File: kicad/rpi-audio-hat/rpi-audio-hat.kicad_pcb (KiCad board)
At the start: 2 copper layers, 65 x 57.6 mm, 14 parts, among them J1 Raspberry_Pi_2_3, J2 Conn_02x20_Counter_Clockwise, J4 Conn_Volume_Slider, J5 Screw_Terminal_01x02, J6 Screw_Terminal_01x02, J7 Screw_Terminal_01x02, SW1 SW_SPDT, U1 PCM5102_breakout, U2 PAM8302A_Adafruit_Board

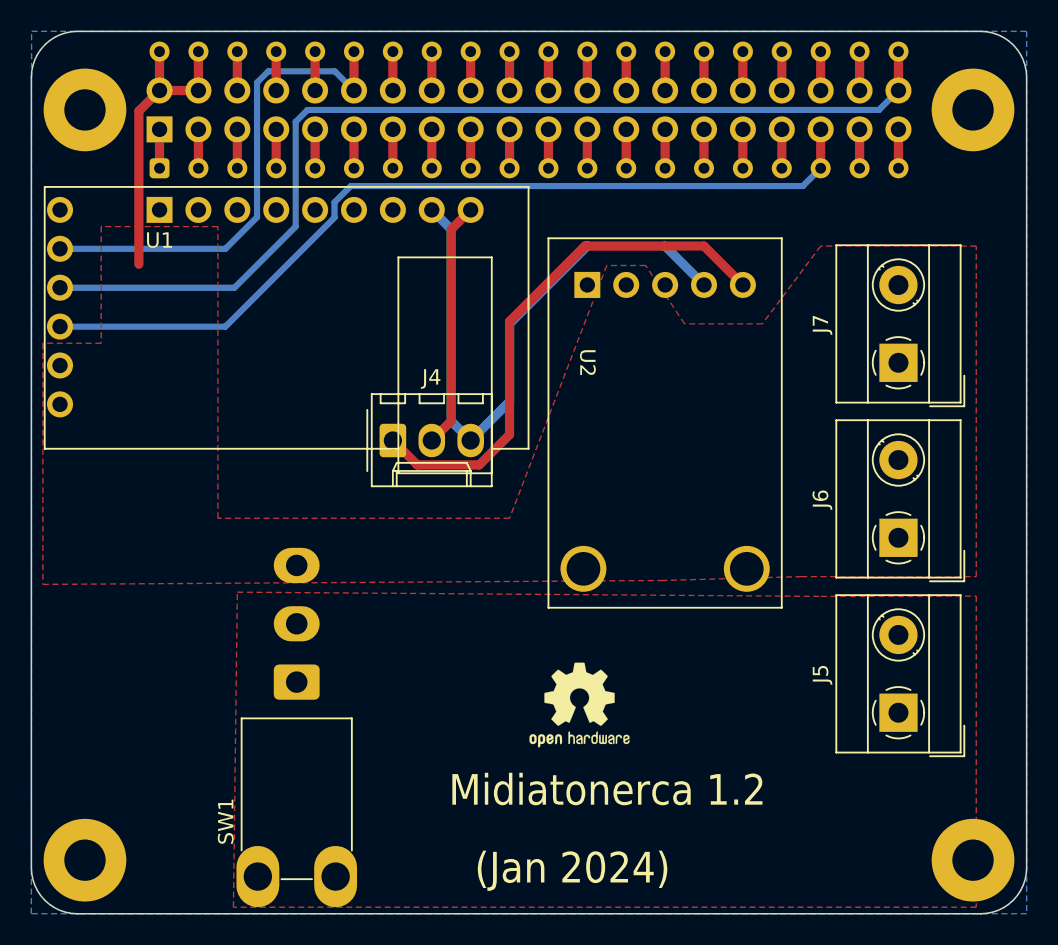
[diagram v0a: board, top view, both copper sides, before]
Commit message: Update PCB for RPi audio hat
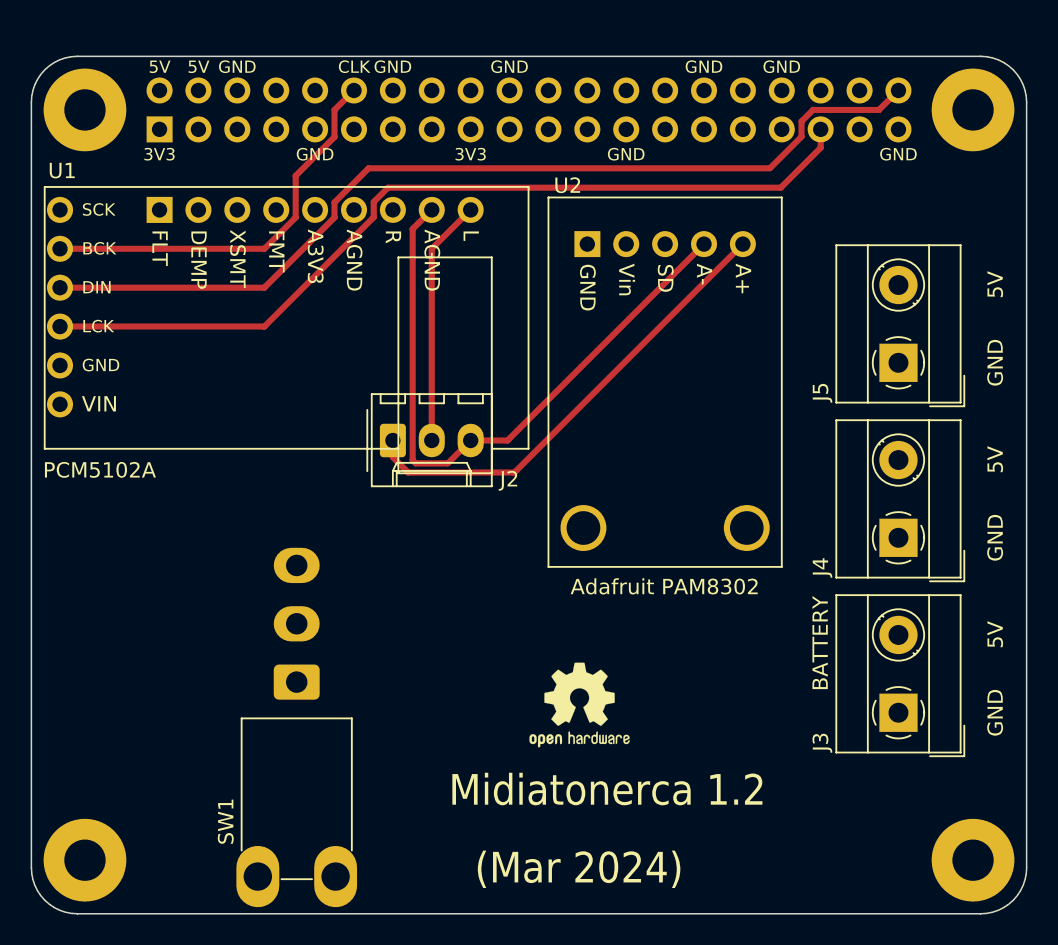
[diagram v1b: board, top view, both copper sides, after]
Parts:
- removed the J2 at (25.4, 27.9)
- U1: footprint Audio_Module:PCM5102_breakout -> MidiatonercaLibrary:PCM5102_breakout
- U2: footprint Audio_Module:PAM8302 -> MidiatonercaLibrary:PAM8302
- moved U2 2.67 mm to (53.3, 32.9)
- renumbered J4 to J2, J5 to J3, J6 to J4, J7 to J5
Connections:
- J1 pad 10: rpi10 -> unconnected-(J1-GPIO15/RXD-Pad10)
- J1 pad 11: rpi11 -> unconnected-(J1-GPIO17-Pad11)
- J1 pad 13: rpi13 -> unconnected-(J1-GPIO27-Pad13)
- J1 pad 15: rpi15 -> unconnected-(J1-GPIO22-Pad15)
- J1 pad 16: rpi16 -> unconnected-(J1-GPIO23-Pad16)
- J1 pad 18: rpi18 -> unconnected-(J1-GPIO24-Pad18)
- J1 pad 19: rpi19 -> unconnected-(J1-MOSI0/GPIO10-Pad19)
- J1 pad 21: rpi21 -> unconnected-(J1-MISO0/GPIO9-Pad21)
- J1 pad 22: rpi22 -> unconnected-(J1-GPIO25-Pad22)
- J1 pad 23: rpi23 -> unconnected-(J1-SCLK0/GPIO11-Pad23)
- J1 pad 24: rpi24 -> unconnected-(J1-~{CE0}/GPIO8-Pad24)
- J1 pad 26: rpi26 -> unconnected-(J1-~{CE1}/GPIO7-Pad26)
- J1 pad 27: rpi27 -> unconnected-(J1-ID_SD/GPIO0-Pad27)
- J1 pad 28: rpi28 -> unconnected-(J1-ID_SC/GPIO1-Pad28)
- J1 pad 29: rpi29 -> unconnected-(J1-GCLK1/GPIO5-Pad29)
- J1 pad 3: rpi03 -> unconnected-(J1-SDA/GPIO2-Pad3)
- J1 pad 31: rpi31 -> unconnected-(J1-GCLK2/GPIO6-Pad31)
- J1 pad 32: rpi32 -> unconnected-(J1-PWM0/GPIO12-Pad32)
- J1 pad 33: rpi33 -> unconnected-(J1-PWM1/GPIO13-Pad33)
- J1 pad 36: rpi36 -> unconnected-(J1-GPIO16-Pad36)
- J1 pad 37: rpi37 -> unconnected-(J1-GPIO26-Pad37)
- J1 pad 38: rpi38 -> unconnected-(J1-GPIO20/MOSI1-Pad38)
- J1 pad 5: rpi05 -> unconnected-(J1-SCL/GPIO3-Pad5)
- J1 pad 7: rpi07 -> unconnected-(J1-GCLK0/GPIO4-Pad7)
- J1 pad 8: rpi08 -> unconnected-(J1-GPIO14/TXD-Pad8)
- J4 pad 2: +5VP -> +5V
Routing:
- net GND: track 20.3 -> 0.00 mm
- net +5V: track 19.5 -> 0.00 mm
- net rpi12: track 32.2 -> 26.1 mm
- net rpi40: track 66.6 -> 61.3 mm
- net +3.3V: track 5.08 -> 0.00 mm
- net Volume A+: track 34.8 -> 30.6 mm
- net rpi37: track 2.54 -> 0.00 mm
- net rpi33: track 2.54 -> 0.00 mm
- net rpi31: track 2.54 -> 0.00 mm
- net rpi29: track 2.54 -> 0.00 mm
- net rpi27: track 2.54 -> 0.00 mm
- net rpi23: track 2.54 -> 0.00 mm
- net rpi21: track 2.54 -> 0.00 mm
- net rpi19: track 2.54 -> 0.00 mm
- net rpi15: track 2.54 -> 0.00 mm
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- added copper zone on In2.Cu, net +5V
- added copper zone on In2.Cu, net +5VP
- added copper zone on In1.Cu, net GND
- removed copper zone on F.Cu, net +5V
- removed copper zone on F.Cu, net +5VP
- removed copper zone on B.Cu, net GND
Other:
- board size 65 x 57.6 mm -> 65 x 56 mm
- copper layers 2 -> 4
- board text added: "(Mar 2024)"
- board text added: "3V3"
- board text added: "5V"
- board text added: "Adafruit PAM8302"
- board text added: "BATTERY"
- board text added: "CLK"
- board text added: "GND"
- board text added: "PCM5102A"
- board text removed: "(Jan 2024)"

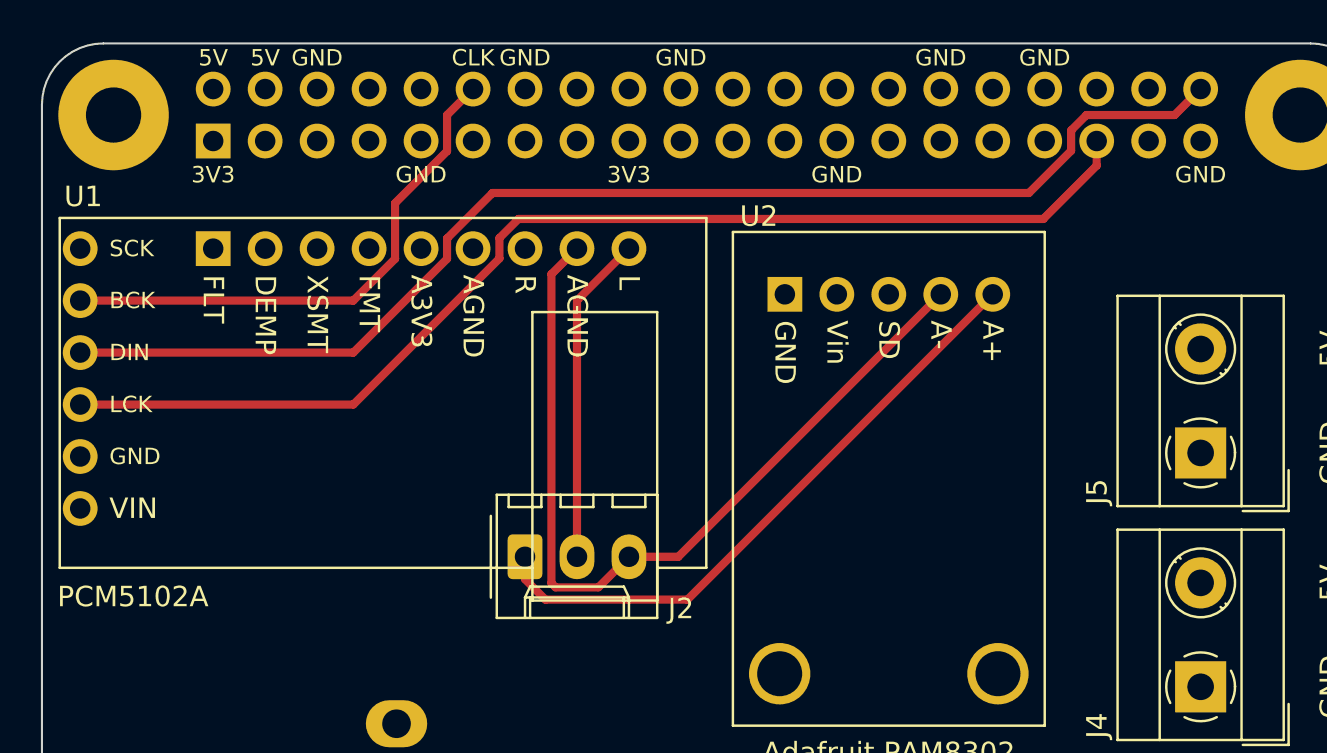
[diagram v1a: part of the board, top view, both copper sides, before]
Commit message: Update RPi hat pcb
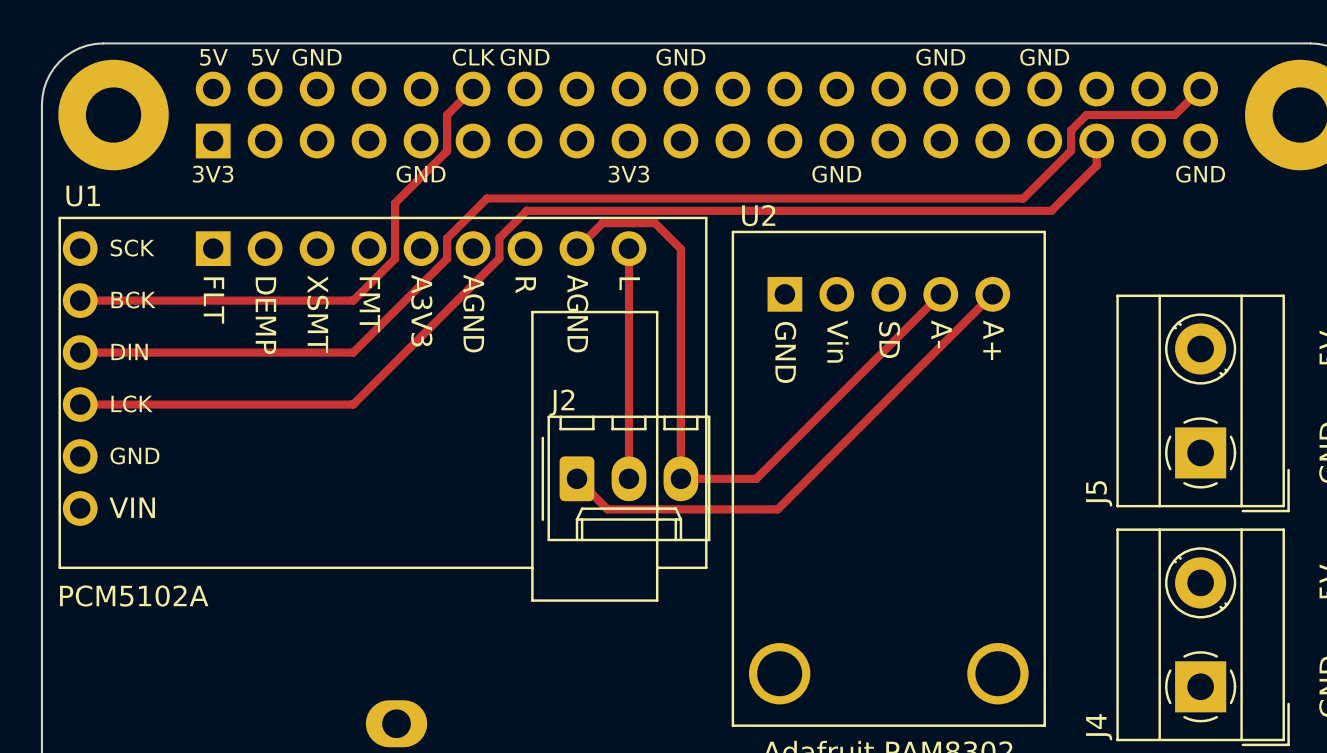
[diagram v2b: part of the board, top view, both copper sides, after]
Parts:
- moved J2 4.58 mm to (43.2, 41.9)
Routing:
- net A-: track 41.9 -> 33.8 mm
- net Volume A+: track 30.6 -> 25.3 mm
- net A+: track 16.1 -> 11.2 mm
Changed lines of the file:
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@@
 		)
 		(fp_text user "AGND"
-			(at 17.78 1.27 -90)
+			(at 17.78 1.27 270)
 			(unlocked yes)
 			(layer "F.SilkS")
 			(effects
 				(font
-					(size 1 1)
+					(size 1 0.95)
 					(thickness 0.1)
 				)
@@
 		)
 		(fp_text user "AGND"
-			(at 12.7 1.27 -90)
+			(at 12.7 1.27 270)
 			(unlocked yes)
 			(layer "F.SilkS")
 			(effects
 				(font
-					(size 1 1)
+					(size 1 0.95)
 					(thickness 0.1)
 				)
@@
 	(footprint "Connector_Molex:Molex_KK-254_AE-6410-03A_1x03_P2.54mm_Vertical"
 		(layer "F.Cu")
-		(at 40.64 45.72)
+		(at 43.18 41.91)
 		(descr "Molex KK-254 Interconnect System, old/engineering part number: AE-6410-03A example for new part number: 22-27-2031, 3 Pins (http://www.molex.com/pdm_docs/sd/022272021_sd.pdf), generated with kicad-footprint-generator")
 		(tags "connector Molex KK-254 vertical")
 		(property "Reference" "J2"
-			(at 7.62 2.54 0)
+			(at -1.27 -3.81 0)
 			(layer "F.SilkS")
 			(effects
@@
 					(thickness 0.15)
 				)
+				(justify left)
 			)
 		)
@@
 			)
 		)
-		(property ki_fp_filters "PinHeader*2x20*P2.54mm*Vertical* PinSocket*2x20*P2.54mm*Vertical*")
-		(sheetname "Root")
-		(sheetfile "rpi-audio-hat.kicad_sch")
 		(attr through_hole)
 		(fp_line
-			(start -3.87 1.33)
-			(end -1.27 1.33)
+			(start -1.27 1.33)
+			(end -3.87 1.33)
 			(stroke
 				(width 0.12)
@@
 		)
 		(fp_line
-			(start -3.87 1.33)
-			(end -3.87 -49.59)
+			(start 1.33 1.33)
+			(end 0 1.33)
 			(stroke
 				(width 0.12)
@@
 		)
 		(fp_line
-			(start -1.27 1.33)
-			(end -1.27 -1.27)
+			(start 1.33 0)
+			(end 1.33 1.33)
 			(stroke
 				(width 0.12)
@@
 		)
 		(fp_line
-			(start 0 1.33)
-			(end 1.33 1.33)
+			(start -1.27 -1.27)
+			(end -1.27 1.33)
 			(stroke
 				(width 0.12)
@@
 		)
 		(fp_line
-			(start 1.33 1.33)
-			(end 1.33 0)
+			(start 1.33 -1.27)
+			(end -1.27 -1.27)
 			(stroke
 				(width 0.12)
@@
 		)
 		(fp_line
-			(start -1.27 -1.27)
-			(end 1.33 -1.27)
+			(start -3.87 -49.59)
+			(end -3.87 1.33)
 			(stroke
 				(width 0.12)
@@
 		)
 		(fp_line
-			(start 1.33 -1.27)
-			(end 1.33 -49.59)
+			(start 1.33 -49.59)
+			(end 1.33 -1.27)
 			(stroke
 				(width 0.12)
@@
 		)
 		(fp_line
-			(start -3.87 -49.59)
-			(end 1.33 -49.59)
+			(start 1.33 -49.59)
+			(end -3.87 -49.59)
 			(stroke
 				(width 0.12)
@@
 		(fp_line
 			(start -4.34 1.8)
-			(end 1.76 1.8)
+			(end -4.34 -50)
 			(stroke
 				(width 0.05)
@@
 		(fp_line
 			(start 1.76 1.8)
-			(end 1.76 -50)
+			(end -4.34 1.8)
 			(stroke
 				(width 0.05)
@@
 		(fp_line
 			(start -4.34 -50)
-			(end -4.34 1.8)
+			(end 1.76 -50)
 			(stroke
 				(width 0.05)
@@
 		(fp_line
 			(start 1.76 -50)
-			(end -4.34 -50)
+			(end 1.76 1.8)
 			(stroke
 				(width 0.05)
@@
 		(fp_line
 			(start -3.81 1.27)
-			(end 0.27 1.27)
+			(end -3.81 -49.53)
 			(stroke
 				(width 0.1)
@@
 		(fp_line
 			(start 0.27 1.27)
-			(end 1.27 0.27)
+			(end -3.81 1.27)
 			(stroke
 				(width 0.1)
@@
 		(fp_line
 			(start 1.27 0.27)
-			(end 1.27 -49.53)
+			(end 0.27 1.27)
 			(stroke
 				(width 0.1)
@@
 		(fp_line
 			(start -3.81 -49.53)
-			(end -3.81 1.27)
+			(end 1.27 -49.53)
 			(stroke
 				(width 0.1)
@@
 		(fp_line
 			(start 1.27 -49.53)
-			(end -3.81 -49.53)
+			(end 1.27 0.27)
 			(stroke
 				(width 0.1)
@@
 		)
 		(fp_text user "${REFERENCE}"
-			(at -1.27 -24.13 0)
+			(at -1.27 -24.13 180)
 			(layer "B.Fab")
 			(effects
@@
 			(pintype "bidirectional")
 		)
-		(model "${KICAD6_3DMODEL_DIR}/Connector_PinSocket_2.54mm.3dshapes/PinSocket_2x20_P2.54mm_Vertical.wrl"
+		(model "${KICAD8_3DMODEL_DIR}/Connector_PinSocket_2.54mm.3dshapes/PinSocket_2x20_P2.54mm_Vertical.wrl"
 			(offset
 				(xyz 0 0 0)
@@
 	)
 	(segment
-		(start 68.58 26.602081)
-		(end 68.58 25.4)
-		(width 0.4)
-		(layer "F.Cu")
-		(net 25)
-	)
-	(segment
-		(start 40.322233 29.21)
-		(end 65.972081 29.21)
+		(start 39.39 31.137767)
+		(end 32.247767 38.28)
 		(width 0.4)
 		(layer "F.Cu")
@@
 	)
 	(segment
-		(start 32.247767 38.28)
-		(end 39.39 31.137767)
+		(start 68.58 26.602081)
+		(end 66.372081 28.81)
 		(width 0.4)
 		(layer "F.Cu")
@@
 	)
 	(segment
-		(start 18.9 38.28)
-		(end 32.247767 38.28)
+		(start 68.58 25.4)
+		(end 68.58 26.602081)
 		(width 0.4)
 		(layer "F.Cu")
@@
 	)
 	(segment
-		(start 65.972081 29.21)
-		(end 68.58 26.602081)
+		(start 66.372081 28.81)
+		(end 40.722233 28.81)
 		(width 0.4)
 		(layer "F.Cu")
@@
 	)
 	(segment
-		(start 39.39 31.137767)
-		(end 39.39 30.142233)
+		(start 32.247767 38.28)
+		(end 18.9 38.28)
 		(width 0.4)
 		(layer "F.Cu")
@@
 	(segment
 		(start 39.39 30.142233)
-		(end 40.322233 29.21)
+		(end 39.39 31.137767)
 		(width 0.4)
 		(layer "F.Cu")
@@
 	)
 	(segment
-		(start 68.082233 24.13)
-		(end 72.39 24.13)
+		(start 40.722233 28.81)
+		(end 39.39 30.142233)
 		(width 0.4)
 		(layer "F.Cu")
-		(net 29)
+		(net 25)
 	)
 	(segment
-		(start 67.33 24.882233)
+		(start 72.39 24.13)
 		(end 68.082233 24.13)
 		(width 0.4)
@@
 	)
 	(segment
-		(start 39.052233 27.94)
-		(end 65.267767 27.94)
+		(start 32.247767 35.74)
+		(end 18.9 35.74)
 		(width 0.4)
 		(layer "F.Cu")
@@
 	)
 	(segment
-		(start 65.267767 27.94)
-		(end 67.33 25.877767)
+		(start 68.082233 24.13)
+		(end 67.33 24.882233)
 		(width 0.4)
 		(layer "F.Cu")
@@
 	)
 	(segment
-		(start 36.83 30.162233)
-		(end 39.052233 27.94)
+		(start 73.66 22.86)
+		(end 72.39 24.13)
 		(width 0.4)
 		(layer "F.Cu")
@@
 	)
 	(segment
-		(start 18.9 35.74)
-		(end 32.247767 35.74)
+		(start 67.33 24.882233)
+		(end 67.33 25.877767)
 		(width 0.4)
 		(layer "F.Cu")
@@
 	)
 	(segment
-		(start 32.247767 35.74)
-		(end 36.83 31.157767)
+		(start 67.33 25.877767)
+		(end 64.997767 28.21)
 		(width 0.4)
 		(layer "F.Cu")
@@
 	)
 	(segment
-		(start 36.83 31.157767)
+		(start 38.782233 28.21)
 		(end 36.83 30.162233)
 		(width 0.4)
@@
 	)
 	(segment
-		(start 67.33 25.877767)
-		(end 67.33 24.882233)
+		(start 36.83 31.157767)
+		(end 32.247767 35.74)
 		(width 0.4)
 		(layer "F.Cu")
@@
 	)
 	(segment
-		(start 72.39 24.13)
-		(end 73.66 22.86)
+		(start 36.83 30.162233)
+		(end 36.83 31.157767)
 		(width 0.4)
 		(layer "F.Cu")
@@
 	)
 	(segment
-		(start 43.18 33.2)
-		(end 43.18 45.72)
+		(start 64.997767 28.21)
+		(end 38.782233 28.21)
 		(width 0.4)
 		(layer "F.Cu")
-		(net 31)
+		(net 29)
 	)
 	(segment
 		(start 45.72 30.66)
-		(end 43.18 33.2)
+		(end 45.72 41.91)
 		(width 0.4)
 		(layer "F.Cu")
@@
 	)
 	(segment
-		(start 44.225 47.215)
-		(end 45.72 45.72)
+		(start 43.18 30.66)
+		(end 44.43 29.41)
 		(width 0.4)
 		(layer "F.Cu")
@@
 	)
 	(segment
-		(start 41.93 31.91)
-		(end 41.93 47.01)
+		(start 48.26 30.68)
+		(end 46.99 29.41)
 		(width 0.4)
 		(layer "F.Cu")
@@
 	)
 	(segment
-		(start 48.133 45.72)
-		(end 45.72 45.72)
+		(start 48.26 41.91)
+		(end 48.26 30.68)
 		(width 0.4)
 		(layer "F.Cu")
@@
 	)
 	(segment
-		(start 41.93 47.01)
-		(end 42.135 47.215)
+		(start 48.26 41.91)
+		(end 51.943 41.91)
 		(width 0.4)
 		(layer "F.Cu")
@@
 	)
 	(segment
-		(start 43.18 30.66)
-		(end 41.93 31.91)
+		(start 44.43 29.41)
+		(end 45.72 29.41)
 		(width 0.4)
 		(layer "F.Cu")
@@
 	)
 	(segment
-		(start 42.135 47.215)
-		(end 44.225 47.215)
+		(start 45.72 29.41)
+		(end 46.99 29.41)
 		(width 0.4)
 		(layer "F.Cu")
@@
 	)
 	(segment
-		(start 60.96 32.893)
-		(end 48.133 45.72)
+		(start 51.943 41.91)
+		(end 60.96 32.893)
 		(width 0.4)
 		(layer "F.Cu")
@@
 	)
 	(segment
-		(start 41.640001 47.815)
-		(end 40.64 46.814999)
-		(width 0.4)
-		(layer "F.Cu")
-		(net 33)
-	)
-	(segment
-		(start 63.5 32.893)
-		(end 48.578 47.815)
+		(start 44.675 43.405)
+		(end 52.988 43.405)
 		(width 0.4)
 		(layer "F.Cu")
@@
 	)
 	(segment
-		(start 48.578 47.815)
-		(end 41.640001 47.815)
+		(start 43.18 41.91)
+		(end 44.675 43.405)
 		(width 0.4)
 		(layer "F.Cu")
@@
 	)
 	(segment
-		(start 40.64 46.814999)
-		(end 40.64 45.72)
+		(start 52.988 43.405)
+		(end 63.5 32.893)
 		(width 0.4)
 		(layer "F.Cu")

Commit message: Work on schematic
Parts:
- removed REF**: OSHW-Logo2_7.3x6mm_SilkScreen, Symbol:OSHW-Logo2_7.3x6mm_SilkScreen
- added C1: 100nF, Capacitor_SMD:C_0603_1608Metric, F.Cu at (94.1, 49.6)
- added C10: 100nF, Capacitor_SMD:C_0603_1608Metric, F.Cu at (98.2, 52.1)
- added C11: 10uF, Capacitor_SMD:C_0603_1608Metric, F.Cu at (98.2, 54.6)
- added C12: 100nF, Capacitor_SMD:C_0603_1608Metric, F.Cu at (98.2, 57.1)
- added C13: 100nF, Capacitor_SMD:C_0603_1608Metric, F.Cu at (98.2, 59.7)
- added C2: 100nF, Capacitor_SMD:C_0603_1608Metric, F.Cu at (94.1, 52.1)
- added C5: 10uF, Capacitor_SMD:C_0603_1608Metric, F.Cu at (94.1, 54.6)
- added C6: 10uF, Capacitor_SMD:C_0603_1608Metric, F.Cu at (94.1, 57.1)
- added C7: 100nF, Capacitor_SMD:C_0603_1608Metric, F.Cu at (94.1, 59.7)
- added C8: 10uF, Capacitor_SMD:C_0603_1608Metric, F.Cu at (94.1, 62.2)
- added C9: 10uF, Capacitor_SMD:C_0603_1608Metric, F.Cu at (98.2, 49.6)
- added R1: 3.9k, Resistor_SMD:R_0603_1608Metric, F.Cu at (98.2, 62.2)
- added R2: 220R, Resistor_SMD:R_0603_1608Metric, F.Cu at (102.2, 49.6)
- added R3: 220R, Resistor_SMD:R_0603_1608Metric, F.Cu at (102.2, 52.1)
- added R4: 100k, Resistor_SMD:R_0603_1608Metric, F.Cu at (102.2, 54.6)
- added R5: 100k, Resistor_SMD:R_0603_1608Metric, F.Cu at (102.2, 57.1)
- added U3: SLM6800, Package_DFN_QFN:QFN-16-1EP_4x4mm_P0.65mm_EP2.15x2.15mm, F.Cu at (107.3, 63.1)
- added U4: PCM5102A, Package_SO:TSSOP-20_4.4x6.5mm_P0.65mm, F.Cu at (96.9, 67.4)
- added U5: MAX98306xDT, Package_DFN_QFN:TDFN-14-1EP_3x3mm_P0.4mm_EP1.78x2.35mm, F.Cu at (107.3, 68.8)
- added U6: PAM8406D, Package_SO:SOP-16_3.9x9.9mm_P1.27mm, F.Cu at (108.4, 54.3)
